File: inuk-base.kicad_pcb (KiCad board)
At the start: 2 copper layers, 100 x 70 mm, 82 parts, among them J1 Conn_02x05_Odd_Even, J2 Conn_01x06, J3 Conn_01x02_Male, J4 Conn_01x02_Male, J5 Conn_01x08, J6 Conn_01x03_Male, J7 Conn_01x03_Male, J8 Conn_01x02_Male, Q1 DMG3406L, Q2 DMG3406L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

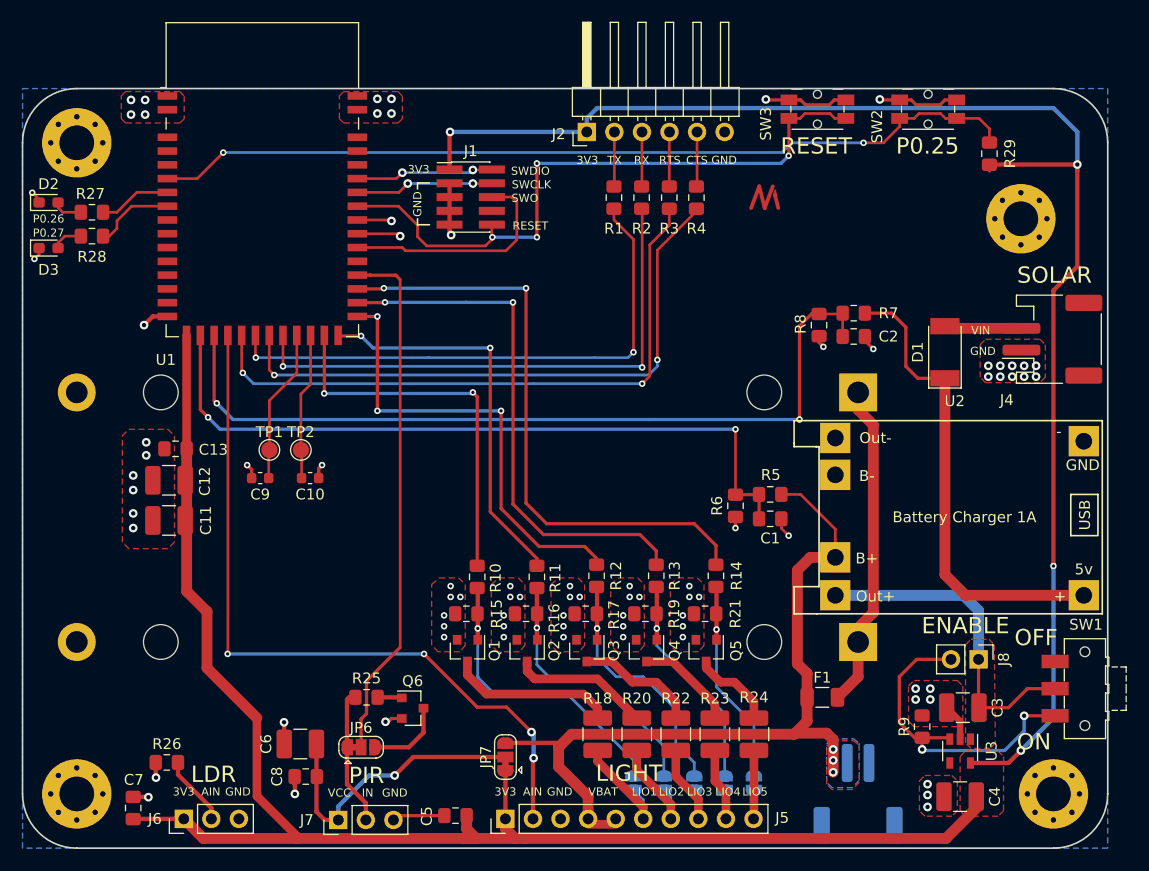
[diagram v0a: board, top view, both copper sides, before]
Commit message: layout and more silk informations
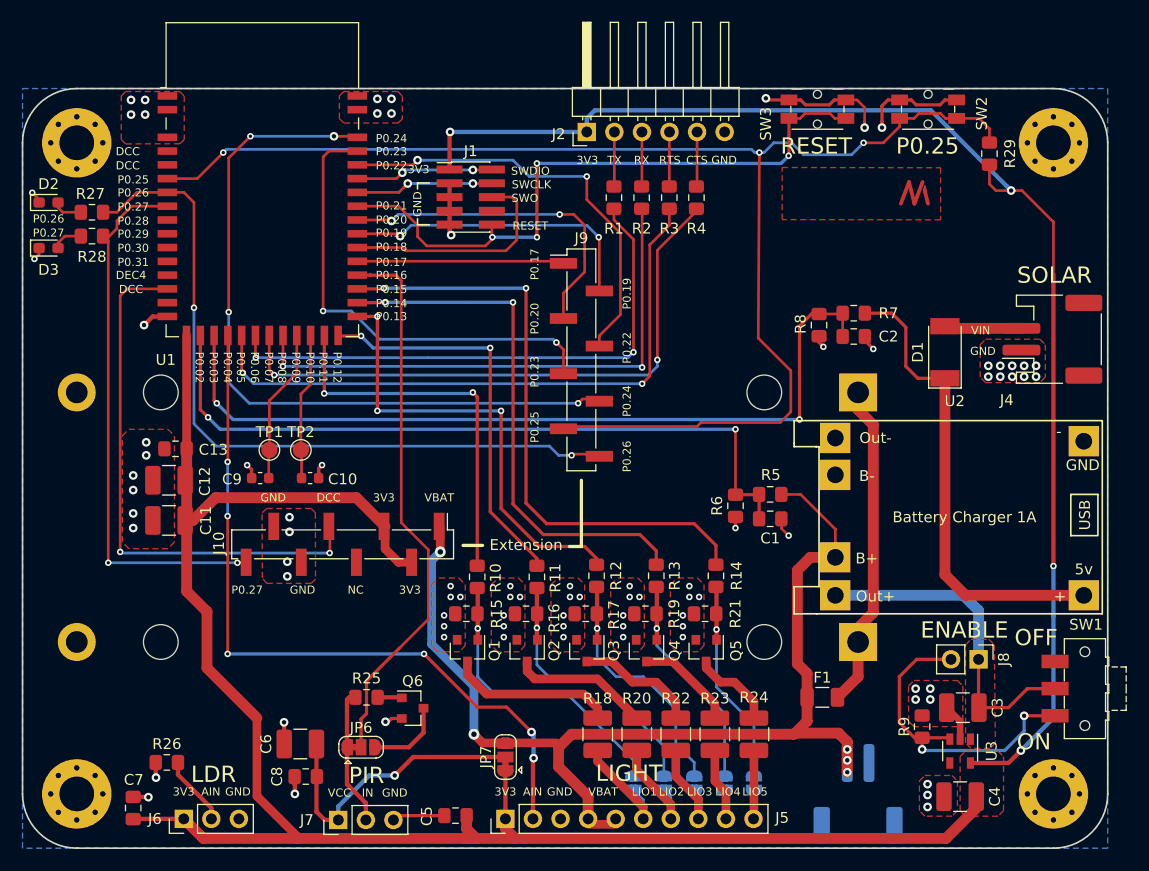
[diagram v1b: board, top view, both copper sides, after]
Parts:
- added J10: Conn_01x08_Male, Connector_PinHeader_2.54mm:PinHeader_1x08_P2.54mm_Vertical_SMD_Pin1Left, F.Cu at (84.5, 117.0)
- added J9: Conn_01x08_Male, Connector_PinHeader_2.54mm:PinHeader_1x08_P2.54mm_Vertical_SMD_Pin1Left, F.Cu at (106.5, 100.0)
- moved U4 13.8 mm to (137.2, 84.6)
- moved H3 7.62 mm to (150.0, 80.0)
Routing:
- net /cpu/P0.24: track 0.00 -> 68.5 mm, vias 0 -> 4
- net /cpu/P0.26: track 6.68 -> 68.5 mm, vias 0 -> 2
- net /cpu/DCC: track 0.00 -> 50.2 mm, vias 0 -> 2
- net /cpu/P0.25: track 81.1 -> 128.9 mm, vias 2 -> 3
- net /cpu/P0.23: track 0.00 -> 43.2 mm, vias 0 -> 2
- net /cpu/P0.27: track 7.48 -> 50.6 mm, vias 0 -> 2
- net /cpu/P0.22: track 0.00 -> 39.5 mm, vias 0 -> 2
- net /cpu/P0.20: track 3.19 -> 30.8 mm, vias 1 -> 2
- net +BATT: track 73.8 -> 99.3 mm, vias 3 -> 5
- net /cpu/P0.19: track 4.04 -> 28.0 mm, vias 1 -> 2
- net /cpu/P0.17: track 0.00 -> 19.0 mm
- net +3V3: track 277.1 -> 290.4 mm
- net GND: track 49.8 -> 55.7 mm, vias 78 -> 83
- net /cpu/pir_input: track 48.7 -> 50.9 mm
- net /cpu/ain2: vias 4 -> 6
- removed copper zone on B.Cu, net +BATT
- removed copper zone on F.Cu, net +BATT
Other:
- board text added: "DCC"
- board text added: "DEC4"
- board text added: "Extension"
- board text added: "Inuk base"
- board text added: "NC"
- board text added: "P0.02"
- board text added: "P0.03"
- board text added: "P0.04"
- board text added: "P0.05"
- board text added: "P0.06"
- board text added: "P0.07"
- board text added: "P0.08"
- board text added: "P0.09"
- board text added: "P0.10"
- board text added: "P0.11"
- board text added: "P0.12"
- board text added: "P0.13"
- board text added: "P0.14"
- board text added: "P0.15"
- board text added: "P0.16"
- board text added: "P0.17"
- board text added: "P0.18"
- board text added: "P0.19"
- board text added: "P0.20"
- board text added: "P0.21"
- board text added: "P0.22"
- board text added: "P0.23"
- board text added: "P0.24"
- board text added: "P0.28"
- board text added: "P0.29"
- board text added: "P0.30"
- board text added: "P0.31"
- board text added: "Rev. 0.9"

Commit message: finished layout, created production files and added readme
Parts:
- D1: value SM4007 -> B230-13-F; footprint Diode_SMD:D_MELF -> Diode_SMD:D_SMB
- J5: footprint Connector_PinHeader_2.54mm:PinHeader_1x10_P2.54mm_Vertical -> Custom:LED_shield; moved to B.Cu
- R27, R28: value 1K -> 1k
- R8: value 2M -> 806k
- moved J5 5.95 mm to (93.5, 142.4), turned to 270 degrees
- moved JP3 5.40 mm to (111.5, 139.0)
- moved JP4 5.40 mm to (114.3, 139.0)
- moved JP5 5.40 mm to (117.0, 139.0)
- moved JP1 5.40 mm to (105.9, 139.0)
- moved JP2 5.40 mm to (108.7, 139.0)
- moved C5 4.70 mm to (93.0, 137.7)
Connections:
- J10 pad 2: +3V3 -> /cpu/AIN5
- J10 pad 4: Net-(J10-Pad4) -> /cpu/AIN6
- J10 pad 6: GND -> /cpu/AIN7
- J6 pad 2: /pir/ldr_sense -> /cpu/ain4
- R26 pad 1: /pir/ldr_sense -> /cpu/ain4
- U1 pad 10: /cpu/ain6 -> /cpu/AIN6
- U1 pad 11: /cpu/ain7 -> /cpu/AIN7
- U1 pad 9: /cpu/ain5 -> /cpu/AIN5
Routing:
- net /cpu/ain4: track 0.00 -> 79.7 mm, vias 0 -> 4
- net /cpu/AIN5: track 0.00 -> 64.9 mm, vias 0 -> 2
- net /cpu/AIN6: track 0.00 -> 46.9 mm, vias 0 -> 4
- net /cpu/AIN7: track 0.00 -> 37.9 mm, vias 0 -> 2
- net /pir/ldr_sense: track 6.47 -> 0.00 mm
- net Net-(J5-Pad10): track 9.02 -> 13.9 mm
- net /light_ctrl/lio_2_sig: track 25.8 -> 21.1 mm
- net /cpu/ain2: track 68.5 -> 64.5 mm, vias 6 -> 5
- net /light_ctrl/lio_3_sig: track 23.7 -> 20.0 mm
- net /light_ctrl/lio_1_sig: track 28.3 -> 25.2 mm
- net /cpu/P0.26: track 68.5 -> 71.3 mm
- net Net-(J5-Pad9): track 9.68 -> 12.4 mm
- net /light_ctrl/lio_4_sig: track 21.1 -> 18.8 mm
- net +3V3: track 290.4 -> 292.0 mm
- net GND: track 55.7 -> 57.3 mm, vias 83 -> 81
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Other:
- board text added: "+"
- board text added: "Rev. 1.0"
- board text removed: "NC"
- board text removed: "Rev. 0.9"
